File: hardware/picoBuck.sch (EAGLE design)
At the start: 37 parts, among them U1 AL8805WS, U2 AL8805WS, U3 AL8805WS

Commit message: Fixed issues from qc feedback
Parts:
- removed CH2, CH3: (no value), SparkFun:M023.5MM_LOCK
- added JP5: M022.54MM_SCREWTERM, SparkFun-Connectors:M022.54MM_SCREWTERM
- added JP6: (no value), SparkFun:M023.5MM_LOCK
- JP3: value M022.54MM_SCREWTERM -> (none); device SparkFun-Connectors:M022.54MM_SCREWTERM -> SparkFun:M023.5MM_LOCK
- renumbered CH1 to JP1
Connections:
- net CTRL_CH1: now also JP5.1; no longer JP4.1
- net CTRL_CH2: now also JP4.2; no longer JP3.2
- net CTRL_CH3: now also JP4.1; no longer JP3.1
- net GND: now also JP5.2, JP6.1; no longer JP2.1, JP4.2
- net N$1: now also JP3.1; no longer CH3.1
- net N$13: now also JP2.1; no longer CH2.1
- net N$16: now also JP3.2; no longer CH3.2
- net N$9: now also JP2.2; no longer CH2.2
- net VIN: now also JP6.2; no longer JP2.2
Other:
- note added: "Close SJ1, SJ2, SJ3 to increase driver current to 670mA."
- moved on the sheet: JP2, JP3, JP4
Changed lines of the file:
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@@
 <part name="L2" library="SparkFun-Passives" deviceset="INDUCTOR" device="BOURNS_SRN6045" value="33uH"/>
 <part name="L3" library="SparkFun-Passives" deviceset="INDUCTOR" device="BOURNS_SRN6045" value="33uH"/>
+<part name="JP6" library="SparkFun" deviceset="M02" device="3.5MM_LOCK"/>
 <part name="JP2" library="SparkFun" deviceset="M02" device="3.5MM_LOCK"/>
-<part name="CH2" library="SparkFun" deviceset="M02" device="3.5MM_LOCK"/>
-<part name="CH1" library="SparkFun" deviceset="M02" device="3.5MM_LOCK"/>
-<part name="CH3" library="SparkFun" deviceset="M02" device="3.5MM_LOCK"/>
+<part name="JP1" library="SparkFun" deviceset="M02" device="3.5MM_LOCK"/>
+<part name="JP3" library="SparkFun" deviceset="M02" device="3.5MM_LOCK"/>
 <part name="C5" library="SparkFun-Capacitors" deviceset="1.0UF-25V-+80/-20(0805)" device="&quot;" value="1.0uF"/>
 <part name="D1" library="SparkFun-DiscreteSemi" deviceset="DIODE-SCHOTTKY" device="-MBRA140" value="MBRA140"/>
@@
 <part name="LOGO2" library="SparkFun-Aesthetics" deviceset="LOGO-SFE" device="NEW"/>
 <part name="FRAME1" library="SparkFun-Aesthetics" deviceset="FRAME-LETTER" device=""/>
-<part name="JP3" library="SparkFun-Connectors" deviceset="M02" device="2.54MM_SCREWTERM" value="M022.54MM_SCREWTERM"/>
 <part name="JP4" library="SparkFun-Connectors" deviceset="M02" device="2.54MM_SCREWTERM" value="M022.54MM_SCREWTERM"/>
+<part name="JP5" library="SparkFun-Connectors" deviceset="M02" device="2.54MM_SCREWTERM" value="M022.54MM_SCREWTERM"/>
 <part name="FID1" library="SparkFun-Aesthetics" deviceset="FIDUCIAL" device="UFIDUCIAL"/>
 <part name="FID2" library="SparkFun-Aesthetics" deviceset="FIDUCIAL" device="UFIDUCIAL"/>
@@
 <text x="238.506" y="6.604" size="3.81" layer="91">11</text>
 <text x="153.924" y="6.35" size="3.81" layer="91">Ethan Zonca/Mike Hord</text>
+<text x="53.34" y="162.56" size="1.778" layer="97">Close SJ1, SJ2, SJ3 to increase
+driver current to 670mA.</text>
 </plain>
 <instances>
@@
 <attribute name="VALUE" x="205.74" y="121.92" size="1.778" layer="96"/>
 </instance>
-<instance part="JP2" gate="G$1" x="111.76" y="55.88" rot="R180"/>
-<instance part="CH2" gate="G$1" x="142.24" y="137.16" rot="R180"/>
-<instance part="CH1" gate="G$1" x="63.5" y="137.16" rot="R180"/>
-<instance part="CH3" gate="G$1" x="220.98" y="139.7" rot="R180"/>
+<instance part="JP6" gate="G$1" x="111.76" y="55.88" rot="R180"/>
+<instance part="JP2" gate="G$1" x="142.24" y="137.16" rot="R180"/>
+<instance part="JP1" gate="G$1" x="63.5" y="137.16" rot="R180"/>
+<instance part="JP3" gate="G$1" x="220.98" y="139.7" rot="R180"/>
 <instance part="C5" gate="G$1" x="203.2" y="137.16"/>
 <instance part="D1" gate="G$1" x="71.12" y="134.62" rot="R90"/>
@@
 <instance part="FRAME1" gate="G$1" x="0" y="0"/>
 <instance part="FRAME1" gate="V" x="147.32" y="0"/>
-<instance part="JP3" gate="G$1" x="111.76" y="81.28" smashed="yes" rot="R180">
+<instance part="JP4" gate="G$1" x="111.76" y="81.28" smashed="yes" rot="R180">
 <attribute name="NAME" x="114.3" y="75.438" size="1.778" layer="95" rot="R180"/>
 </instance>
-<instance part="JP4" gate="G$1" x="111.76" y="68.58" smashed="yes" rot="R180">
+<instance part="JP5" gate="G$1" x="111.76" y="68.58" smashed="yes" rot="R180">
 <attribute name="NAME" x="114.3" y="62.738" size="1.778" layer="95" rot="R180"/>
 </instance>
@@
 </segment>
 <segment>
-<pinref part="JP2" gate="G$1" pin="1"/>
+<pinref part="JP6" gate="G$1" pin="1"/>
 <wire x1="104.14" y1="55.88" x2="101.6" y2="55.88" width="0.1524" layer="91"/>
 <label x="101.6" y="55.88" size="1.27" layer="95" rot="R180" xref="yes"/>
 </segment>
 <segment>
-<pinref part="JP4" gate="G$1" pin="2"/>
+<pinref part="JP5" gate="G$1" pin="2"/>
 <wire x1="104.14" y1="66.04" x2="101.6" y2="66.04" width="0.1524" layer="91"/>
 <label x="101.6" y="66.04" size="1.27" layer="95" rot="R180" xref="yes"/>
@@
 </segment>
 <segment>
-<pinref part="JP2" gate="G$1" pin="2"/>
+<pinref part="JP6" gate="G$1" pin="2"/>
 <wire x1="104.14" y1="53.34" x2="101.6" y2="53.34" width="0.1524" layer="91"/>
 <label x="101.6" y="53.34" size="1.27" layer="95" rot="R180" xref="yes"/>
@@
 <junction x="124.46" y="129.54"/>
 <pinref part="L2" gate="G$1" pin="2"/>
-<pinref part="CH2" gate="G$1" pin="2"/>
+<pinref part="JP2" gate="G$1" pin="2"/>
 <wire x1="134.62" y1="134.62" x2="134.62" y2="129.54" width="0.1524" layer="91"/>
 </segment>
@@
 <net name="N$13" class="0">
 <segment>
-<pinref part="CH2" gate="G$1" pin="1"/>
+<pinref part="JP2" gate="G$1" pin="1"/>
 <wire x1="127" y1="142.24" x2="129.54" y2="142.24" width="0.1524" layer="91"/>
 <wire x1="129.54" y1="142.24" x2="134.62" y2="142.24" width="0.1524" layer="91"/>
@@
 <junction x="45.72" y="129.54"/>
 <pinref part="L1" gate="G$1" pin="2"/>
-<pinref part="CH1" gate="G$1" pin="2"/>
+<pinref part="JP1" gate="G$1" pin="2"/>
 <wire x1="55.88" y1="134.62" x2="55.88" y2="129.54" width="0.1524" layer="91"/>
 </segment>
@@
 <net name="N$11" class="0">
 <segment>
-<pinref part="CH1" gate="G$1" pin="1"/>
+<pinref part="JP1" gate="G$1" pin="1"/>
 <wire x1="48.26" y1="142.24" x2="50.8" y2="142.24" width="0.1524" layer="91"/>
 <wire x1="50.8" y1="142.24" x2="55.88" y2="142.24" width="0.1524" layer="91"/>
@@
 <junction x="203.2" y="132.08"/>
 <pinref part="L3" gate="G$1" pin="2"/>
-<pinref part="CH3" gate="G$1" pin="2"/>
+<pinref part="JP3" gate="G$1" pin="2"/>
 <wire x1="213.36" y1="137.16" x2="213.36" y2="132.08" width="0.1524" layer="91"/>
 <pinref part="C5" gate="G$1" pin="2"/>
@@
 </segment>
 <segment>
-<pinref part="JP4" gate="G$1" pin="1"/>
+<pinref part="JP5" gate="G$1" pin="1"/>
 <wire x1="104.14" y1="68.58" x2="101.6" y2="68.58" width="0.1524" layer="91"/>
 <label x="101.6" y="68.58" size="1.27" layer="95" rot="R180" xref="yes"/>
@@
 </segment>
 <segment>
-<pinref part="JP3" gate="G$1" pin="2"/>
+<pinref part="JP4" gate="G$1" pin="2"/>
 <wire x1="104.14" y1="78.74" x2="101.6" y2="78.74" width="0.1524" layer="91"/>
 <label x="101.6" y="78.74" size="1.27" layer="95" rot="R180" xref="yes"/>
@@
 </segment>
 <segment>
-<pinref part="JP3" gate="G$1" pin="1"/>
+<pinref part="JP4" gate="G$1" pin="1"/>
 <wire x1="104.14" y1="81.28" x2="101.6" y2="81.28" width="0.1524" layer="91"/>
 <label x="101.6" y="81.28" size="1.27" layer="95" rot="R180" xref="yes"/>
@@
 <pinref part="C5" gate="G$1" pin="1"/>
 <wire x1="203.2" y1="144.78" x2="203.2" y2="142.24" width="0.1524" layer="91"/>
-<pinref part="CH3" gate="G$1" pin="1"/>
+<pinref part="JP3" gate="G$1" pin="1"/>
 <wire x1="208.28" y1="144.78" x2="213.36" y2="144.78" width="0.1524" layer="91"/>
 <wire x1="213.36" y1="144.78" x2="213.36" y2="139.7" width="0.1524" layer="91"/>

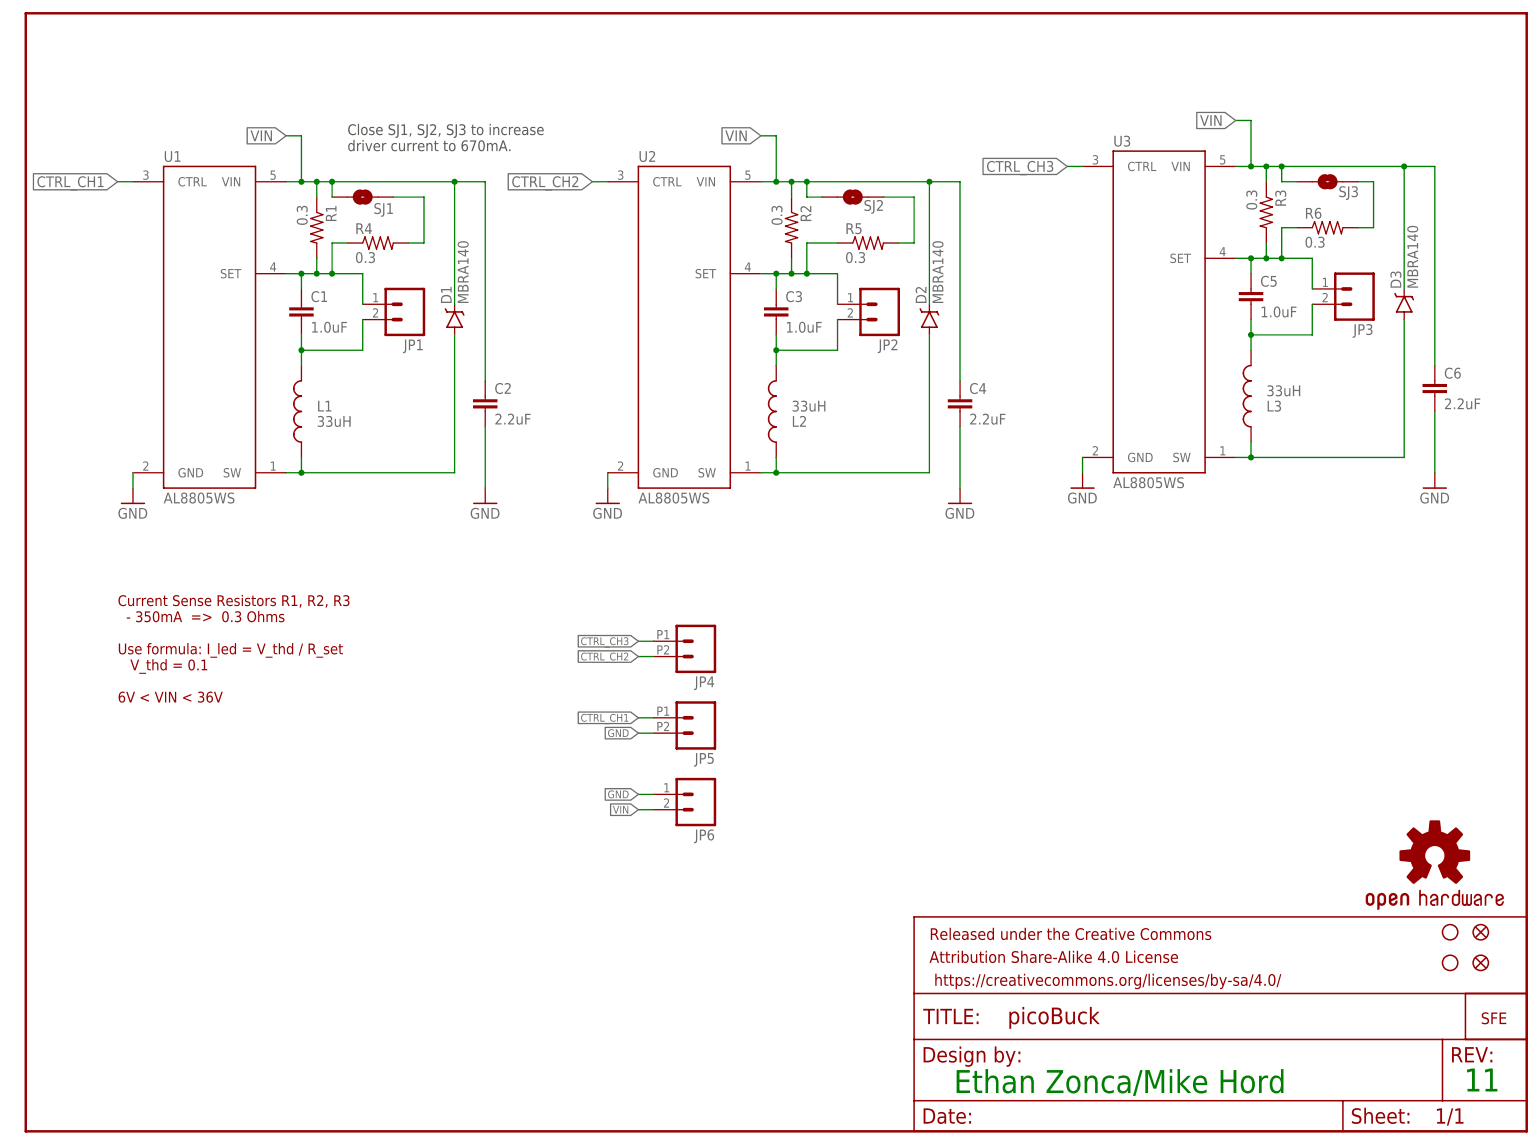
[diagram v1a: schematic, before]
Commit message: Added some silk to back of board
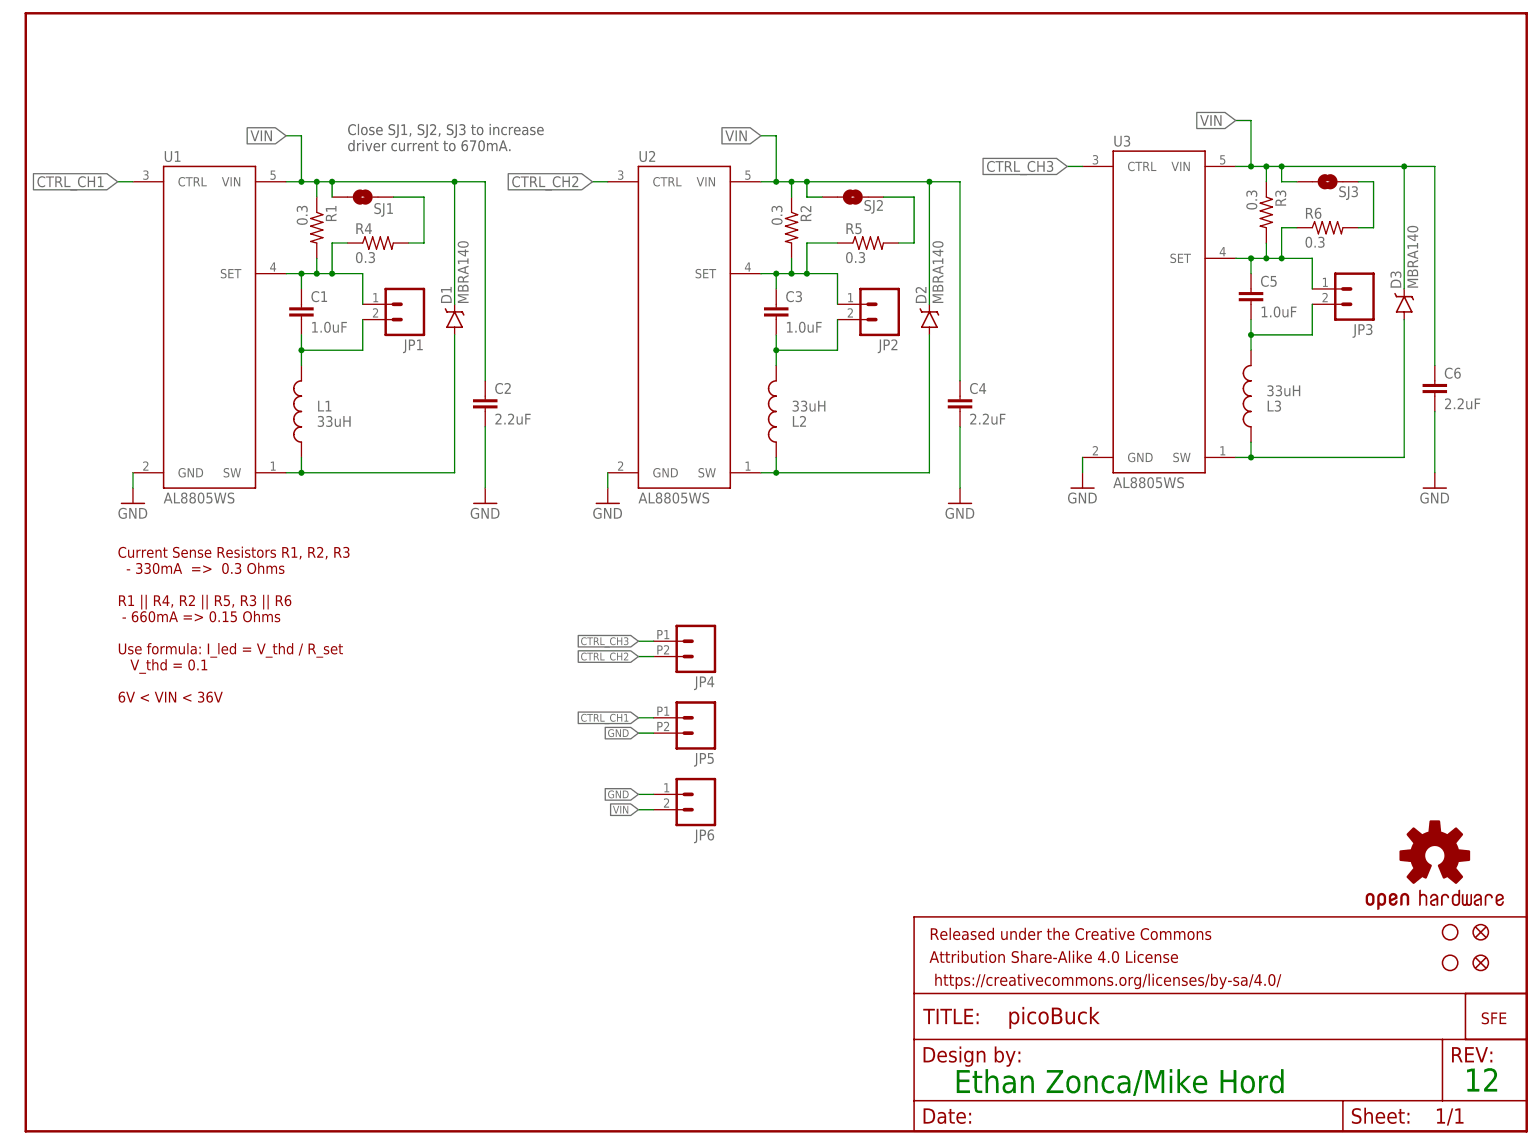
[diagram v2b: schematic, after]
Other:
- note added: "12"
- note added: "Current Sense Resistors R1, R2, R3 - 330mA => 0.3 Ohms R1 || R4, R2 || R5, R3 || R6 - 660mA => 0.15 Ohms Use formula: I_led = V_thd / R_set V_thd = 0.1 6V < VIN < 36V"
- note removed: "11"
- note removed: "Current Sense Resistors R1, R2, R3 - 350mA => 0.3 Ohms Use formula: I_led = V_thd / R_set V_thd = 0.1 6V < VIN < 36V"
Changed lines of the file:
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@@
 <plain>
 <text x="15.24" y="71.12" size="1.778" layer="94">Current Sense Resistors R1, R2, R3
-  - 350mA  =&gt;  0.3 Ohms
+  - 330mA  =&gt;  0.3 Ohms
+R1 || R4, R2 || R5, R3 || R6
+ - 660mA =&gt; 0.15 Ohms
 Use formula: I_led = V_thd / R_set
    V_thd = 0.1
 6V &lt; VIN &lt; 36V</text>
-<text x="238.506" y="6.604" size="3.81" layer="91">11</text>
+<text x="238.506" y="6.604" size="3.81" layer="91">12</text>
 <text x="153.924" y="6.35" size="3.81" layer="91">Ethan Zonca/Mike Hord</text>
 <text x="53.34" y="162.56" size="1.778" layer="97">Close SJ1, SJ2, SJ3 to increase

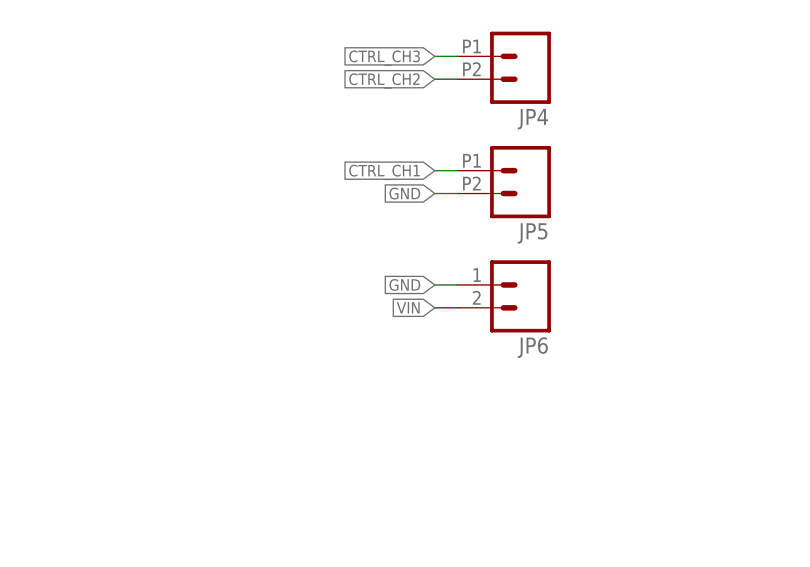
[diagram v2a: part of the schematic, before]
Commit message: Center text on center screw term, add gnd symbols to JP4/5
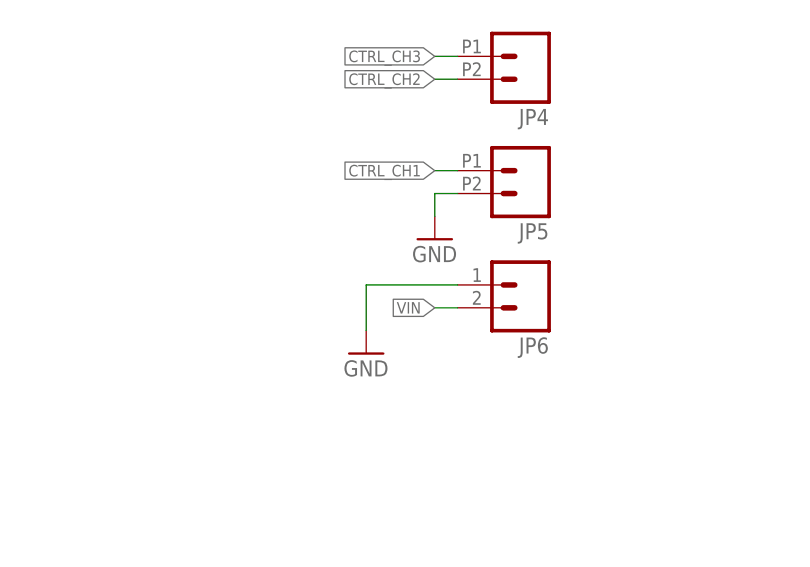
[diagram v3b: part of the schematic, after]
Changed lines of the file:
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@@
 <part name="STANDOFF1" library="SparkFun-Electromechanical" deviceset="STAND-OFF" device=""/>
 <part name="STANDOFF2" library="SparkFun-Electromechanical" deviceset="STAND-OFF" device=""/>
+<part name="GND2" library="SparkFun" deviceset="GND" device=""/>
+<part name="GND3" library="SparkFun" deviceset="GND" device=""/>
 </parts>
 <sheets>
@@
 <instance part="STANDOFF1" gate="G$1" x="236.22" y="27.94"/>
 <instance part="STANDOFF2" gate="G$1" x="236.22" y="33.02"/>
+<instance part="GND2" gate="1" x="93.98" y="48.26"/>
+<instance part="GND3" gate="1" x="101.6" y="60.96"/>
 </instances>
 <busses>
@@
 </segment>
 <segment>
-<pinref part="JP6" gate="G$1" pin="1"/>
-<wire x1="104.14" y1="55.88" x2="101.6" y2="55.88" width="0.1524" layer="91"/>
-<label x="101.6" y="55.88" size="1.27" layer="95" rot="R180" xref="yes"/>
+<pinref part="JP5" gate="G$1" pin="2"/>
+<wire x1="104.14" y1="66.04" x2="101.6" y2="66.04" width="0.1524" layer="91"/>
+<pinref part="GND3" gate="1" pin="GND"/>
+<wire x1="101.6" y1="63.5" x2="101.6" y2="66.04" width="0.1524" layer="91"/>
 </segment>
 <segment>
-<pinref part="JP5" gate="G$1" pin="2"/>
-<wire x1="104.14" y1="66.04" x2="101.6" y2="66.04" width="0.1524" layer="91"/>
-<label x="101.6" y="66.04" size="1.27" layer="95" rot="R180" xref="yes"/>
+<pinref part="JP6" gate="G$1" pin="1"/>
+<wire x1="104.14" y1="55.88" x2="93.98" y2="55.88" width="0.1524" layer="91"/>
+<pinref part="GND2" gate="1" pin="GND"/>
+<wire x1="93.98" y1="50.8" x2="93.98" y2="55.88" width="0.1524" layer="91"/>
 </segment>
 </net>
